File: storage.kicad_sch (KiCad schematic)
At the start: 5 parts, among them J14 DM3CS-SF, U7 MX25V4006EM1I-13G

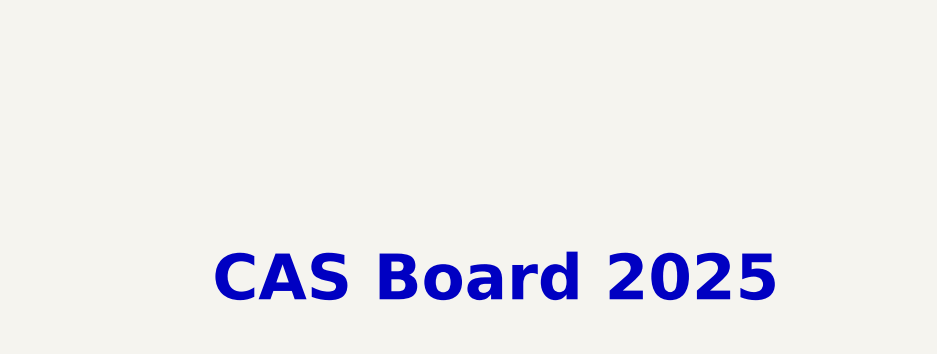
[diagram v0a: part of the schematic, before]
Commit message: remove camera power and interface headers and pins from schematic and PCB
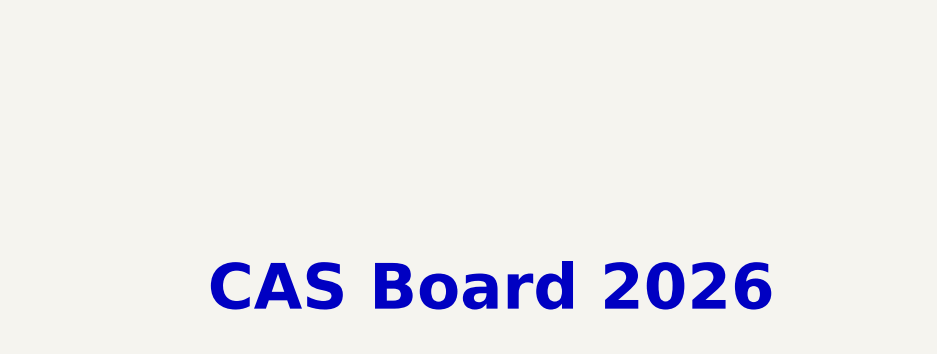
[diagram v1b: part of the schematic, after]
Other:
- note added: "CAS Board 2026"
- note removed: "CAS Board 2025"
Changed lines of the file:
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@@
 		)
 	)
-	(text "CAS Board 2025\n\n"
+	(text "CAS Board 2026"
 		(exclude_from_sim no)
-		(at 209.55 177.8 0)
+		(at 209.042 174.752 0)
 		(effects
 			(font
